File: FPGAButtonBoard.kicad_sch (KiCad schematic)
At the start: 31 parts, among them J1 Conn_02x20_Odd_Even, J2 Analog Discovery 2, SW1 SW_DIP_x08, SW2 SW_DIP_x08, SW3 SW_Push, SW4 SW_Push, SW5 SW_Push, SW6 SW_Push, SW7 SW_Push, SW8 SW_SPST

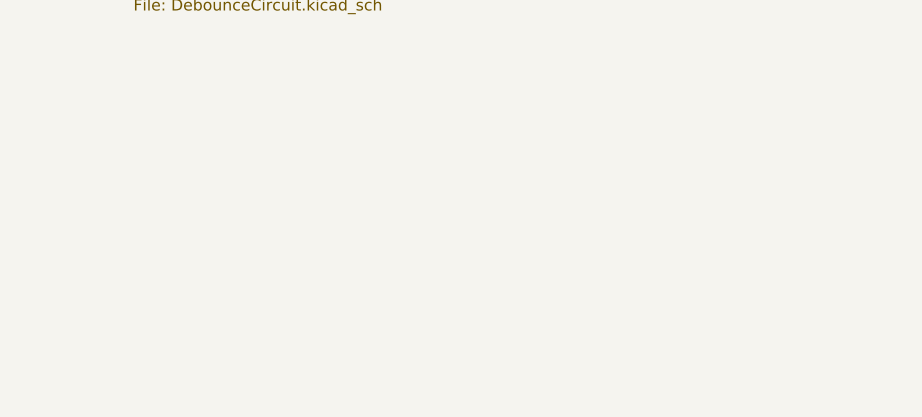
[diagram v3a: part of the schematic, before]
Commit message: Adicionado os furos de montagem. Definidos os footprints
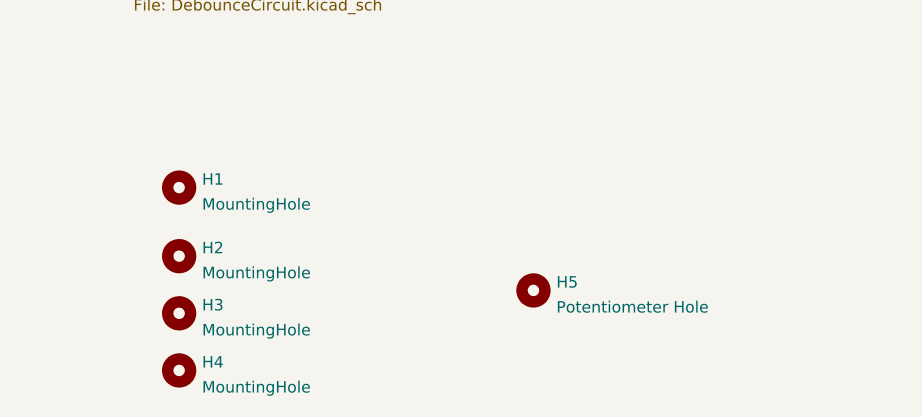
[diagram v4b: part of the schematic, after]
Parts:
- added H1, H2, H3, H4: MountingHole, MountingHole:MountingHole_3.2mm_M3, symbol Mechanical:MountingHole
- added H5: Potentiometer Hole, MountingHole:MountingHole_8.4mm_M8, symbol Mechanical:MountingHole
- SW3, SW4, SW5, SW6, SW7: footprint Button_Switch_THT:SW_PUSH-12mm_Wuerth-430476085716 -> Button_Switch_THT:SW_PUSH_6mm
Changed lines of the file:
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@@
     (property "Reference" "SW5" (id 0) (at 43.18 149.86 0))
     (property "Value" "SW_Push" (id 1) (at 43.18 152.4 0))
-    (property "Footprint" "Button_Switch_THT:SW_PUSH-12mm_Wuerth-430476085716" (id 2) (at 43.18 152.4 0)
+    (property "Footprint" "Button_Switch_THT:SW_PUSH_6mm" (id 2) (at 43.18 152.4 0)
       (effects (font (size 1.27 1.27)) hide)
     )
@@
     (pin "1")
   )
+  (symbol (lib_id "Mechanical:MountingHole") (at 96.52 173.99 0) (unit 1)
+    (in_bom yes) (on_board yes) (fields_autoplaced)
+    (property "Reference" "H1" (id 0) (at 99.06 173.0815 0)
+      (effects (font (size 1.27 1.27)) (justify left))
+    )
+    (property "Value" "MountingHole" (id 1) (at 99.06 175.8566 0)
+      (effects (font (size 1.27 1.27)) (justify left))
+    )
+    (property "Footprint" "MountingHole:MountingHole_3.2mm_M3" (id 2) (at 96.52 173.99 0)
+      (effects (font (size 1.27 1.27)) hide)
+    )
+    (property "Datasheet" "~" (id 3) (at 96.52 173.99 0)
+      (effects (font (size 1.27 1.27)) hide)
+    )
+  )
+  (symbol (lib_id "Mechanical:MountingHole") (at 96.52 194.31 0) (unit 1)
+    (in_bom yes) (on_board yes) (fields_autoplaced)
+    (property "Reference" "H4" (id 0) (at 99.06 193.4015 0)
+      (effects (font (size 1.27 1.27)) (justify left))
+    )
+    (property "Value" "MountingHole" (id 1) (at 99.06 196.1766 0)
+      (effects (font (size 1.27 1.27)) (justify left))
+    )
+    (property "Footprint" "MountingHole:MountingHole_3.2mm_M3" (id 2) (at 96.52 194.31 0)
+      (effects (font (size 1.27 1.27)) hide)
+    )
+    (property "Datasheet" "~" (id 3) (at 96.52 194.31 0)
+      (effects (font (size 1.27 1.27)) hide)
+    )
+  )
   (symbol (lib_id "Device:R") (at 82.55 92.71 0) (unit 1)
     (in_bom yes) (on_board yes) (fields_autoplaced)
@@
     (property "Reference" "SW3" (id 0) (at 41.91 127 0))
     (property "Value" "SW_Push" (id 1) (at 41.91 129.54 0))
-    (property "Footprint" "Button_Switch_THT:SW_PUSH-12mm_Wuerth-430476085716" (id 2) (at 41.91 129.54 0)
+    (property "Footprint" "Button_Switch_THT:SW_PUSH_6mm" (id 2) (at 41.91 129.54 0)
       (effects (font (size 1.27 1.27)) hide)
     )
@@
     (property "Reference" "SW6" (id 0) (at 43.18 162.56 0))
     (property "Value" "SW_Push" (id 1) (at 43.18 165.1 0))
-    (property "Footprint" "Button_Switch_THT:SW_PUSH-12mm_Wuerth-430476085716" (id 2) (at 43.18 165.1 0)
+    (property "Footprint" "Button_Switch_THT:SW_PUSH_6mm" (id 2) (at 43.18 165.1 0)
       (effects (font (size 1.27 1.27)) hide)
     )
@@
     (property "Reference" "SW7" (id 0) (at 44.45 172.72 0))
     (property "Value" "SW_Push" (id 1) (at 44.45 175.26 0))
-    (property "Footprint" "Button_Switch_THT:SW_PUSH-12mm_Wuerth-430476085716" (id 2) (at 44.45 175.26 0)
+    (property "Footprint" "Button_Switch_THT:SW_PUSH_6mm" (id 2) (at 44.45 175.26 0)
       (effects (font (size 1.27 1.27)) hide)
     )
@@
     (property "Reference" "SW4" (id 0) (at 43.18 138.43 0))
     (property "Value" "SW_Push" (id 1) (at 43.18 140.97 0))
-    (property "Footprint" "Button_Switch_THT:SW_PUSH-12mm_Wuerth-430476085716" (id 2) (at 43.18 140.97 0)
+    (property "Footprint" "Button_Switch_THT:SW_PUSH_6mm" (id 2) (at 43.18 140.97 0)
       (effects (font (size 1.27 1.27)) hide)
     )
@@
     (pin "1")
     (pin "2")
+  )
+  (symbol (lib_id "Mechanical:MountingHole") (at 96.52 187.96 0) (unit 1)
+    (in_bom yes) (on_board yes) (fields_autoplaced)
+    (property "Reference" "H3" (id 0) (at 99.06 187.0515 0)
+      (effects (font (size 1.27 1.27)) (justify left))
+    )
+    (property "Value" "MountingHole" (id 1) (at 99.06 189.8266 0)
+      (effects (font (size 1.27 1.27)) (justify left))
+    )
+    (property "Footprint" "MountingHole:MountingHole_3.2mm_M3" (id 2) (at 96.52 187.96 0)
+      (effects (font (size 1.27 1.27)) hide)
+    )
+    (property "Datasheet" "~" (id 3) (at 96.52 187.96 0)
+      (effects (font (size 1.27 1.27)) hide)
+    )
+  )
+  (symbol (lib_id "Mechanical:MountingHole") (at 135.89 185.42 0) (unit 1)
+    (in_bom yes) (on_board yes) (fields_autoplaced)
+    (property "Reference" "H5" (id 0) (at 138.43 184.5115 0)
+      (effects (font (size 1.27 1.27)) (justify left))
+    )
+    (property "Value" "Potentiometer Hole" (id 1) (at 138.43 187.2866 0)
+      (effects (font (size 1.27 1.27)) (justify left))
+    )
+    (property "Footprint" "MountingHole:MountingHole_8.4mm_M8" (id 2) (at 135.89 185.42 0)
+      (effects (font (size 1.27 1.27)) hide)
+    )
+    (property "Datasheet" "~" (id 3) (at 135.89 185.42 0)
+      (effects (font (size 1.27 1.27)) hide)
+    )
   )
   (symbol (lib_id "Device:R") (at 144.78 134.62 90) (unit 1)
@@
     (pin "1")
     (pin "2")
+  )
+  (symbol (lib_id "Mechanical:MountingHole") (at 96.52 181.61 0) (unit 1)
+    (in_bom yes) (on_board yes) (fields_autoplaced)
+    (property "Reference" "H2" (id 0) (at 99.06 180.7015 0)
+      (effects (font (size 1.27 1.27)) (justify left))
+    )
+    (property "Value" "MountingHole" (id 1) (at 99.06 183.4766 0)
+      (effects (font (size 1.27 1.27)) (justify left))
+    )
+    (property "Footprint" "MountingHole:MountingHole_3.2mm_M3" (id 2) (at 96.52 181.61 0)
+      (effects (font (size 1.27 1.27)) hide)
+    )
+    (property "Datasheet" "~" (id 3) (at 96.52 181.61 0)
+      (effects (font (size 1.27 1.27)) hide)
+    )
   )
   (symbol (lib_id "Connector_Generic:Conn_02x20_Odd_Even") (at 195.58 71.12 0) (unit 1)
@@
       (reference "C8") (unit 1) (value "100nF") (footprint "Capacitor_THT:C_Rect_L4.6mm_W3.0mm_P2.50mm_MKS02_FKP02")
     )
+    (path "/36f20f2b-df3d-4bc7-a369-fb3ef715bff8"
+      (reference "H1") (unit 1) (value "MountingHole") (footprint "MountingHole:MountingHole_3.2mm_M3")
+    )
+    (path "/f65c01d8-b9be-489f-97a3-3806780e3977"
+      (reference "H2") (unit 1) (value "MountingHole") (footprint "MountingHole:MountingHole_3.2mm_M3")
+    )
+    (path "/d1eb6e98-7158-4a94-a118-b1e0b7d61df6"
+      (reference "H3") (unit 1) (value "MountingHole") (footprint "MountingHole:MountingHole_3.2mm_M3")
+    )
+    (path "/3acdf624-e7cf-4bcf-8952-16c522a15621"
+      (reference "H4") (unit 1) (value "MountingHole") (footprint "MountingHole:MountingHole_3.2mm_M3")
+    )
+    (path "/d3318490-1137-4881-bb77-fc7848f27e89"
+      (reference "H5") (unit 1) (value "Potentiometer Hole") (footprint "MountingHole:MountingHole_8.4mm_M8")
+    )
     (path "/f6a5cab3-78e5-4acf-8c67-f401df2846d0"
       (reference "J1") (unit 1) (value "Conn_02x20_Odd_Even") (footprint "Connector_PinSocket_2.54mm:PinSocket_2x20_P2.54mm_Vertical")
@@
     )
     (path "/be813dec-c91f-4c06-808b-c742fd6baf99/5e67fd59-cd40-4944-86ed-116074a90f19"
-      (reference "RV1") (unit 1) (value "1M") (footprint "Potentiometer_THT:Potentiometer_Alps_RK09K_Single_Horizontal")
+      (reference "RV1") (unit 1) (value "1M") (footprint "Potentiometer_THT:Potentiometer_Alps_RK163_Single_Horizontal")
     )
     (path "/ed5c770a-74c6-457f-8ffc-d111f7deac9f"
@@
     )
     (path "/4623e300-a2f0-4676-9002-80ce11e8810e"
-      (reference "SW3") (unit 1) (value "SW_Push") (footprint "Button_Switch_THT:SW_PUSH-12mm_Wuerth-430476085716")
+      (reference "SW3") (unit 1) (value "SW_Push") (footprint "Button_Switch_THT:SW_PUSH_6mm")
     )
     (path "/d023e863-19d9-4bf1-82d8-a0404610c60a"
-      (reference "SW4") (unit 1) (value "SW_Push") (footprint "Button_Switch_THT:SW_PUSH-12mm_Wuerth-430476085716")
+      (reference "SW4") (unit 1) (value "SW_Push") (footprint "Button_Switch_THT:SW_PUSH_6mm")
     )
     (path "/0ee787c5-feea-42b6-b161-98ebfb2ec781"
-      (reference "SW5") (unit 1) (value "SW_Push") (footprint "Button_Switch_THT:SW_PUSH-12mm_Wuerth-430476085716")
+      (reference "SW5") (unit 1) (value "SW_Push") (footprint "Button_Switch_THT:SW_PUSH_6mm")
     )
     (path "/a3f0ca4f-9c21-4094-a54c-a244b198f1c3"
-      (reference "SW6") (unit 1) (value "SW_Push") (footprint "Button_Switch_THT:SW_PUSH-12mm_Wuerth-430476085716")
+      (reference "SW6") (unit 1) (value "SW_Push") (footprint "Button_Switch_THT:SW_PUSH_6mm")
     )
     (path "/b44c932c-ecad-4643-b8c8-0e300eaaa8cd"
-      (reference "SW7") (unit 1) (value "SW_Push") (footprint "Button_Switch_THT:SW_PUSH-12mm_Wuerth-430476085716")
+      (reference "SW7") (unit 1) (value "SW_Push") (footprint "Button_Switch_THT:SW_PUSH_6mm")
     )
     (path "/63df2d4e-1a26-4902-af50-405053ca09d5"

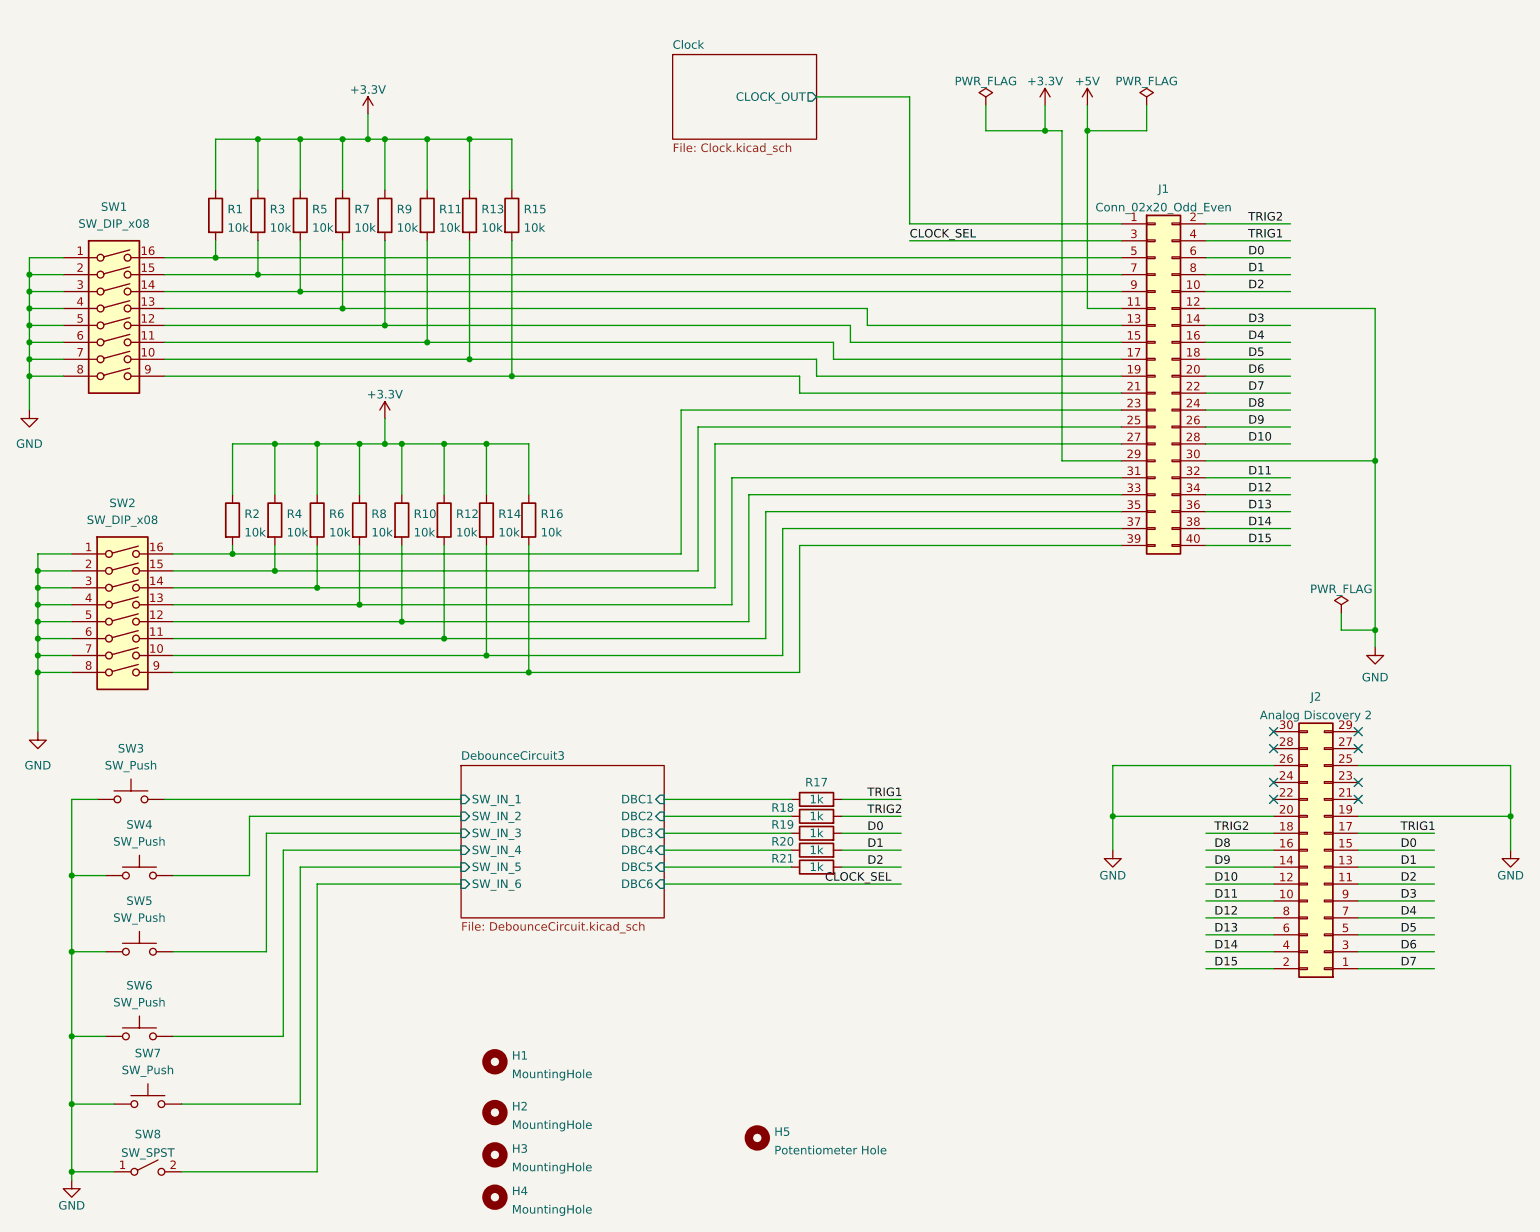
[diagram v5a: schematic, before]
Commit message: Corrigido o botão de seleção de Clock e valores dos capacitores.
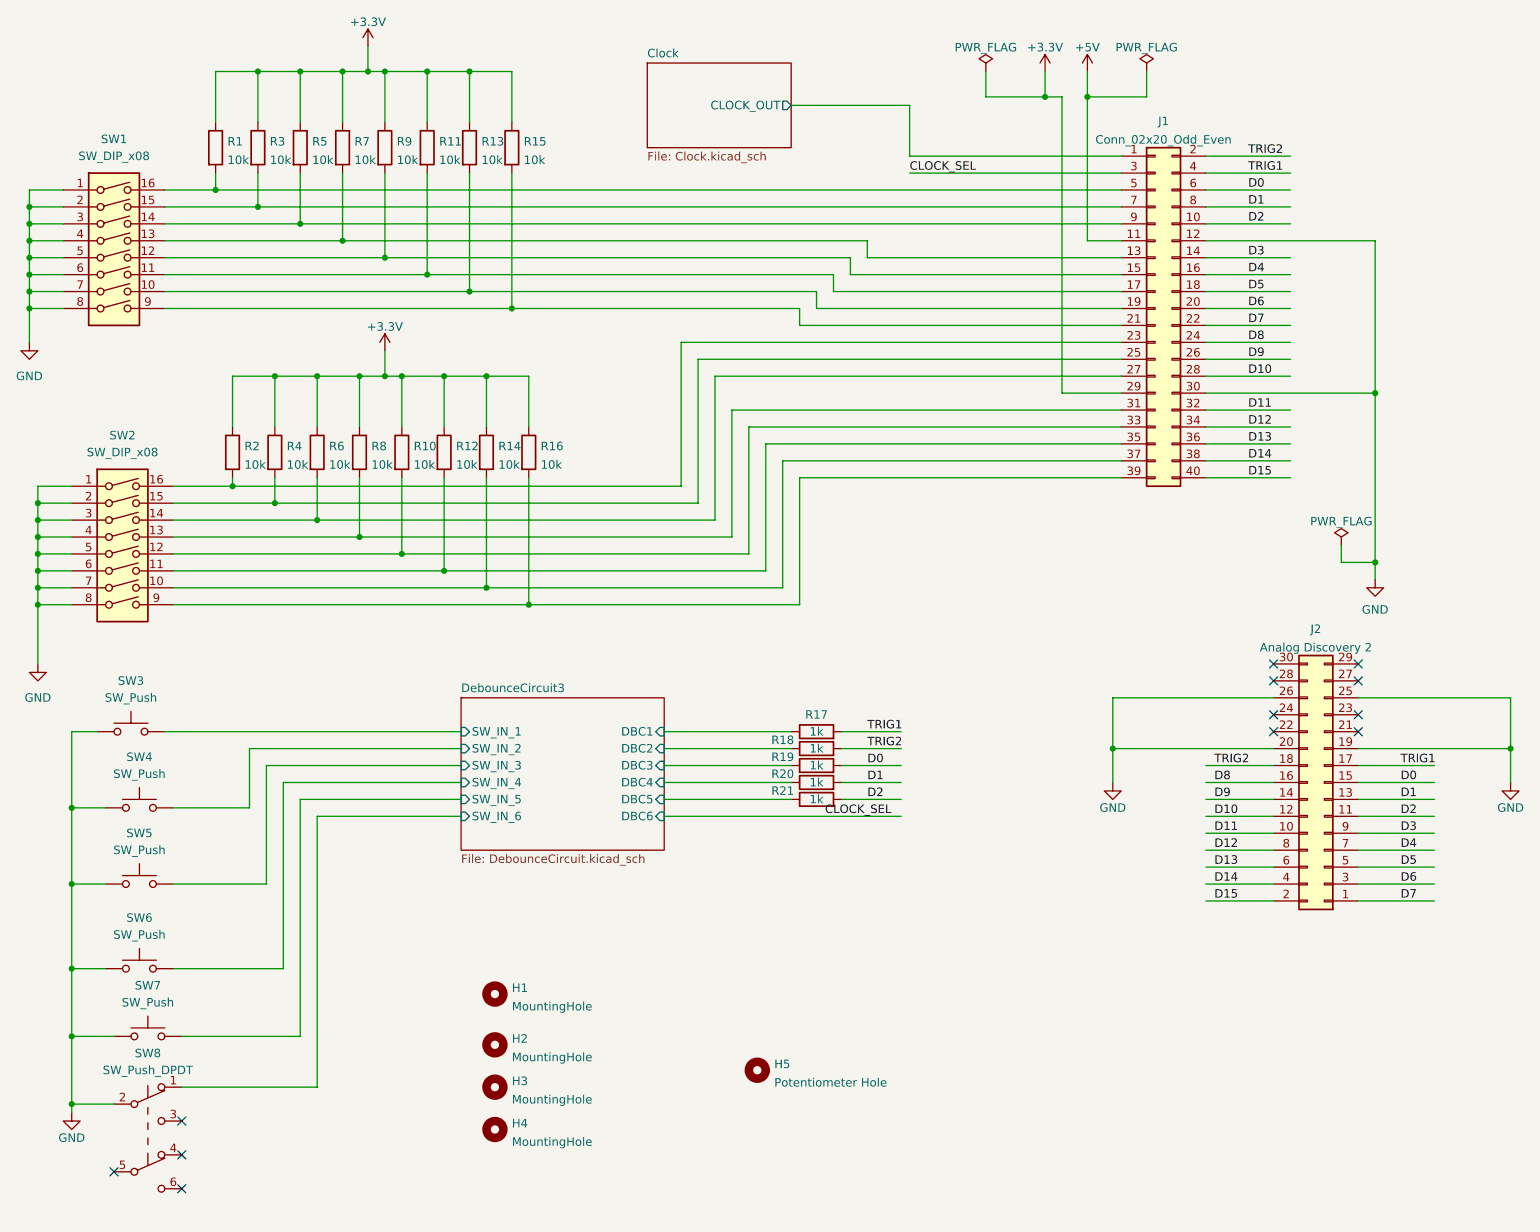
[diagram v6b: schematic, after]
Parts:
- removed SW8: SW_SPST, Button_Switch_THT:SW_PUSH_6mm, symbol Switch:SW_SPST
- added SW8: SW_Push_DPDT, Logo:Nidec_Copal_SH-7010C_Mod, symbol Switch:SW_Push_DPDT
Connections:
- net DebounceCircuit3/SW_IN_6: now also SW8.1 (A)
- net GND: now also SW8.2 (B)
- no-connect marks 8 -> 12
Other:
- moved on the sheet: H1, H2, H3, H4, H5, J1, J2, R1, R10, R11, R12, R13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

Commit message: Atualizado os valores dos capacitores
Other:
- note added: "TODO Próx. Versão: - Aumentar o tamanho das ilhas (R e C) - Aumentar o tamanho dos capacitores eletrolíticos (C1) - Trocar o footprint do botão Sel. Clock"
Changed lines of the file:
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@@
   (title_block
     (title "FGPA Input Board")
+    (rev "1.1")
     (company "Ailton Luiz Dias Siqueira Junior")
   )
@@
   (wire (pts (xy 92.71 25.4) (xy 99.06 25.4))
     (stroke (width 0) (type default) (color 0 0 0 0))
+  )
+  (text "TODO Próx. Versão:\n- Aumentar o tamanho das ilhas (R e C)\n- Aumentar o tamanho dos capacitores eletrolíticos (C1)\n- Trocar o footprint do botão Sel. Clock"
+    (at 177.8 175.26 0)
+    (effects (font (size 1.27 1.27)) (justify left bottom))
   )
   (label "D0" (at 209.55 43.18 0)
@@
     )
     (path "/be813dec-c91f-4c06-808b-c742fd6baf99/541dbd43-e7cd-463a-a9cb-2ceef0945b55"
-      (reference "C1") (unit 1) (value "10uF") (footprint "Capacitor_THT:CP_Radial_D4.0mm_P2.00mm")
+      (reference "C1") (unit 1) (value "47uF") (footprint "Capacitor_THT:CP_Radial_D4.0mm_P2.00mm")
     )
     (path "/be813dec-c91f-4c06-808b-c742fd6baf99/9291be3e-f07e-489b-8cee-2fa887e19ffd"
@@
     )
     (path "/510535f1-0e55-4f79-baad-3bc8f34dbe6b/adcf1a5d-9042-4cd4-b986-04d0eb8b42f1"
-      (reference "C3") (unit 1) (value "47nF") (footprint "Capacitor_THT:C_Rect_L7.0mm_W3.5mm_P5.00mm")
+      (reference "C3") (unit 1) (value "100nF") (footprint "Capacitor_THT:C_Rect_L7.0mm_W3.5mm_P5.00mm")
     )
     (path "/510535f1-0e55-4f79-baad-3bc8f34dbe6b/e4e3cd2d-ffbd-457f-afb3-abfa6377e1e7"
-      (reference "C4") (unit 1) (value "47nF") (footprint "Capacitor_THT:C_Rect_L7.0mm_W3.5mm_P5.00mm")
+      (reference "C4") (unit 1) (value "100nF") (footprint "Capacitor_THT:C_Rect_L7.0mm_W3.5mm_P5.00mm")
     )
     (path "/510535f1-0e55-4f79-baad-3bc8f34dbe6b/d315b2c5-b679-49b2-8df9-6bd9e33cdc3d"
-      (reference "C5") (unit 1) (value "47nF") (footprint "Capacitor_THT:C_Rect_L7.0mm_W3.5mm_P5.00mm")
+      (reference "C5") (unit 1) (value "100nF") (footprint "Capacitor_THT:C_Rect_L7.0mm_W3.5mm_P5.00mm")
     )
     (path "/510535f1-0e55-4f79-baad-3bc8f34dbe6b/89d6be03-feb1-423c-895b-e5cd5a376d58"
-      (reference "C6") (unit 1) (value "47nF") (footprint "Capacitor_THT:C_Rect_L7.0mm_W3.5mm_P5.00mm")
+      (reference "C6") (unit 1) (value "100nF") (footprint "Capacitor_THT:C_Rect_L7.0mm_W3.5mm_P5.00mm")
     )
     (path "/510535f1-0e55-4f79-baad-3bc8f34dbe6b/52828580-849a-4f96-9efb-3247ae3513ac"
-      (reference "C7") (unit 1) (value "47nF") (footprint "Capacitor_THT:C_Rect_L7.0mm_W3.5mm_P5.00mm")
+      (reference "C7") (unit 1) (value "100nF") (footprint "Capacitor_THT:C_Rect_L7.0mm_W3.5mm_P5.00mm")
     )
     (path "/510535f1-0e55-4f79-baad-3bc8f34dbe6b/6fe3410f-6def-4b50-9c0a-a61d2f243405"
-      (reference "C8") (unit 1) (value "47nF") (footprint "Capacitor_THT:C_Rect_L7.0mm_W3.5mm_P5.00mm")
+      (reference "C8") (unit 1) (value "100nF") (footprint "Capacitor_THT:C_Rect_L7.0mm_W3.5mm_P5.00mm")
     )
     (path "/510535f1-0e55-4f79-baad-3bc8f34dbe6b/fdc41eae-4b30-43fe-aa73-4ef1b20eb03d"
